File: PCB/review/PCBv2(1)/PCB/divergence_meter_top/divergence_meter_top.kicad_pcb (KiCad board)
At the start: 2 copper layers, 137.7 x 56.4 mm, 14 parts

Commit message: reviewing top board
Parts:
- JT1: value Conn_01x10 -> Conn_01x12; footprint Connector_PinHeader_2.54mm:PinHeader_1x10_P2.54mm_Vertical -> Connector_PinHeader_2.54mm:PinHeader_1x12_P2.54mm_Vertical; moved to F.Cu
- moved JT1 6.38 mm to (125.7, 130.6), turned to 90 degrees
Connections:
- JT1 pad 10: +1V5 -> GND

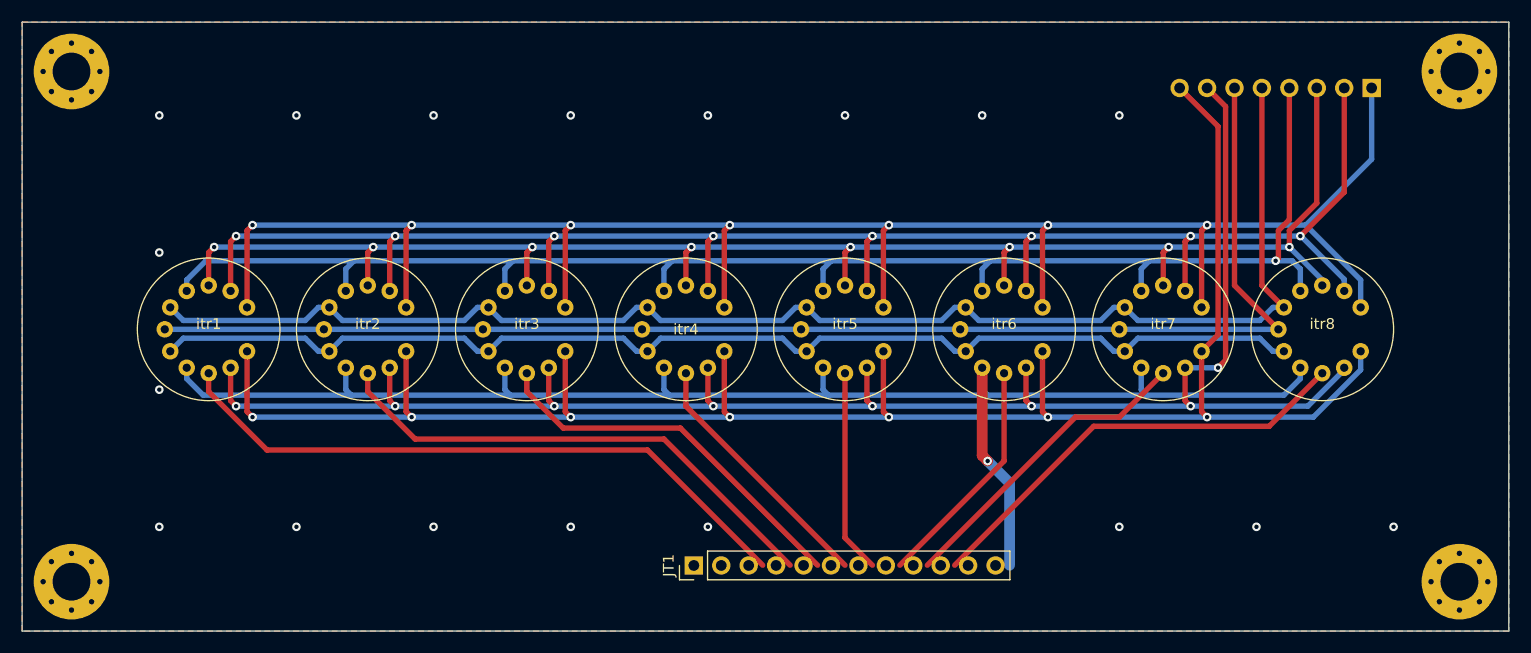
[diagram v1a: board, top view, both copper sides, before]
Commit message: testing silkscreen images
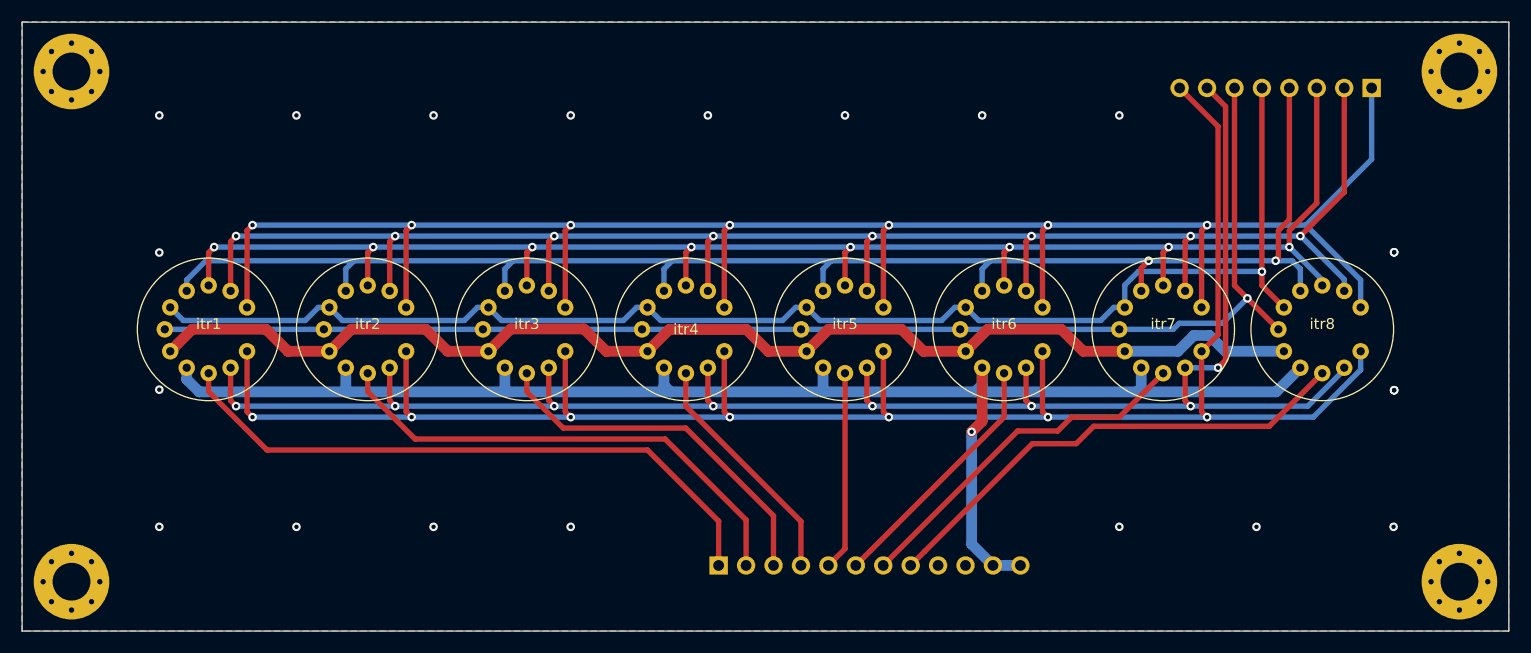
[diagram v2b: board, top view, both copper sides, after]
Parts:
- added G***: LOGO, LOGO, B.Cu at (161.3, 90.8)
- JT1: moved to B.Cu
- moved JT1 2.30 mm to (128.0, 130.6), turned to -90 degrees
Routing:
- net GND: track 110.1 -> 114.5 mm, vias 18 -> 21
- net Net-(itr8-Pad9): track 41.4 -> 45.5 mm
- net Net-(itr7-Pad9): track 29.2 -> 33.3 mm
- net Net-(itr6-Pad9): track 21.8 -> 23.5 mm
- net Net-(JT2-Pad6): track 127.2 -> 125.5 mm, vias 0 -> 1
- net Net-(itr1-Pad9): track 59.7 -> 58.0 mm
- net Net-(itr4-Pad9): track 23.9 -> 22.2 mm
- net Net-(itr2-Pad9): track 47.5 -> 45.9 mm
- net Net-(itr3-Pad9): track 35.3 -> 33.9 mm
- net Net-(JT2-Pad5): track 131.3 -> 130.9 mm, vias 0 -> 1
- net Net-(JT2-Pad4): vias 1 -> 2
